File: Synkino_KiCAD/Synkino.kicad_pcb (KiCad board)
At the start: 2 copper layers, 93.3 x 82.3 mm, 183 parts, among them J1 Pwr, J10 EYE8_OUT, J11 EYE4_OUT, J12 2.5mm, J13 EYE5_OUT, J2 2.5mm, J3 3.5mm, J4 Micro_SD_Card_Det_Hirose_DM3AT, J5 EYE1_OUT, J6 EYE6_OUT, J7 EYE2_OUT, J8 EYE7_OUT, J9 EYE3_OUT, Q1 IRF7319, Q2 BC847, Q3 IRLML2244, SW1 SW_Push, SW2 Rotary_Encoder_Switch, SW3 SW_Push, U1 MCP1702T-5002E/MB, U10 ATMEGA328P-AU, U11 QRE1113, U12 QRE1113, U13 QRE1113, U14 QRE1113, U15 QRE1113, U16 QRE1113, U17 24LC256, U18 QRE1113, U2 ATMEGA328P-AU, U3 74HC4050, U4 SPIOLED128x64, U5 AP7312-1833W6-7, U6 74HC14, U7 VS1053B, U8 MAX4741, U9 QRE1113, X1 FTDIconn, X2 ICSP, X3 FTDIconn, X4 ICSP, Y1 16Mhz, Y2 12.288MHz, Y3 16Mhz

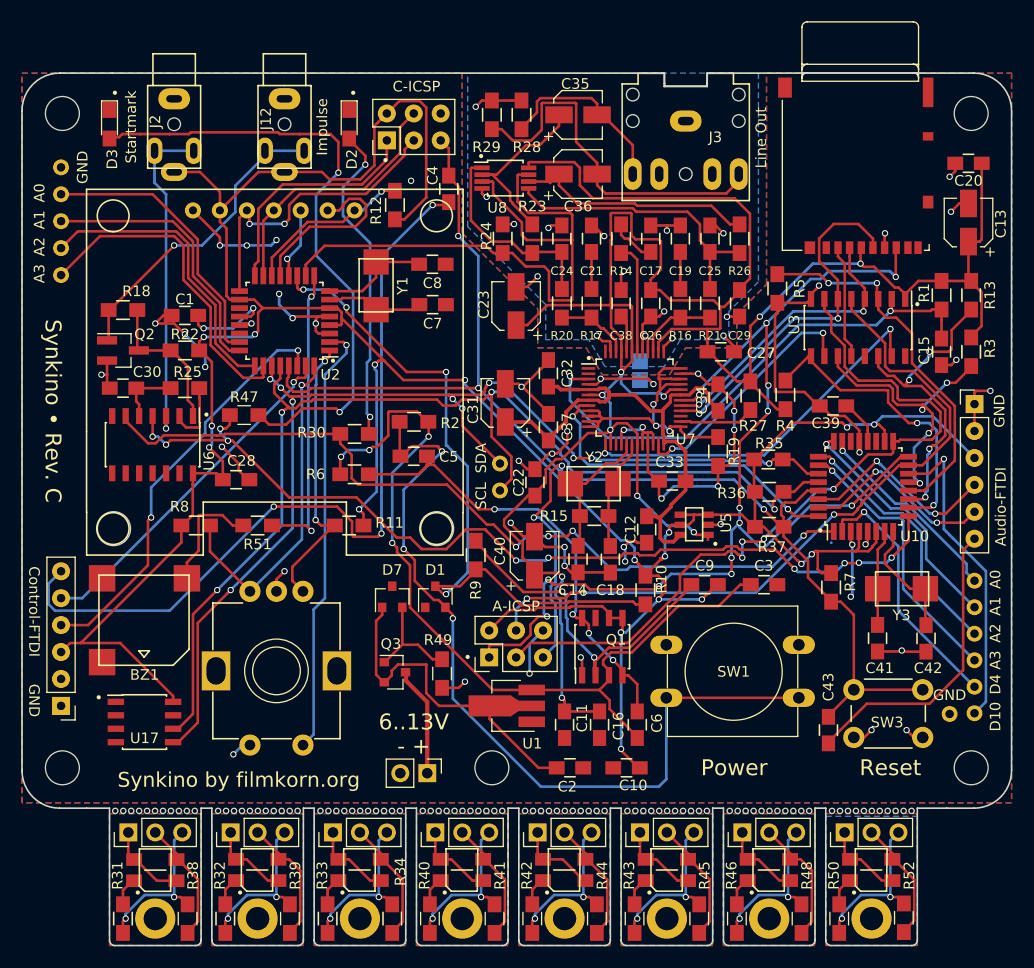
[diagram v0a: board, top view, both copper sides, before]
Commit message: Fixing traces too close to screws
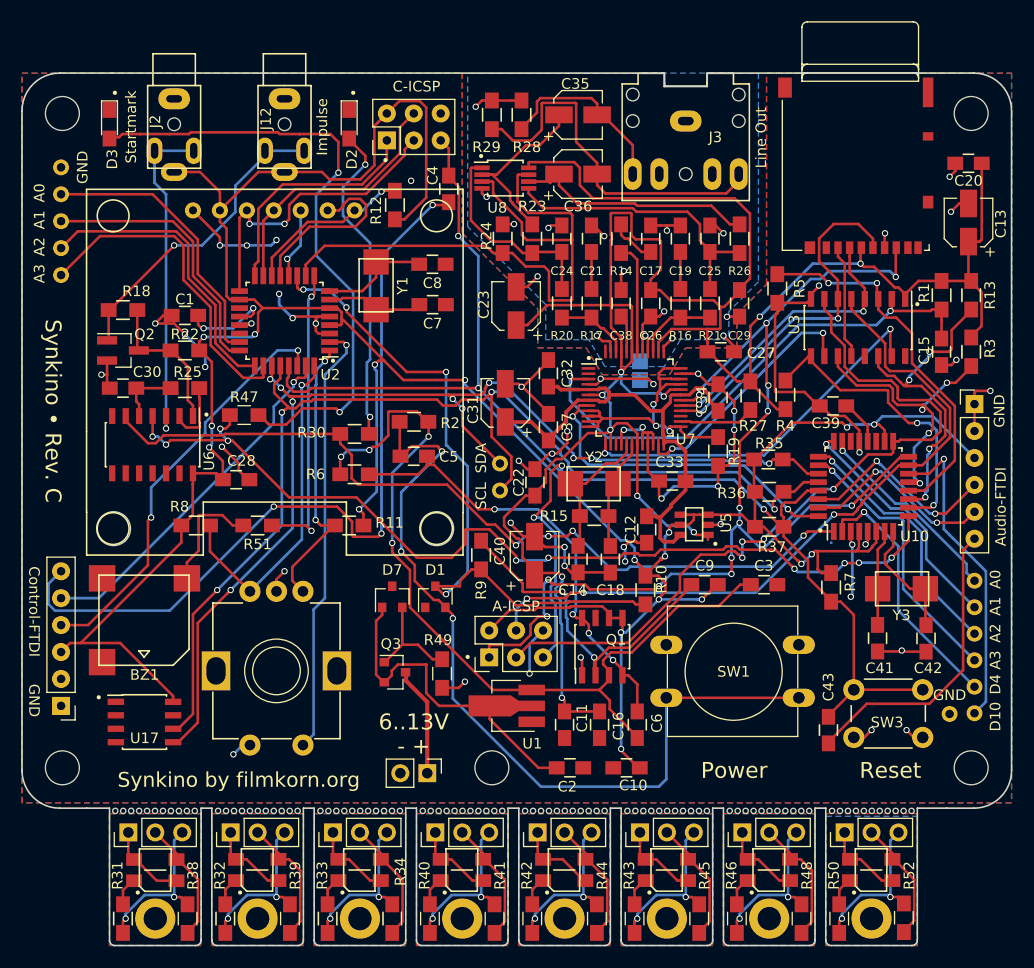
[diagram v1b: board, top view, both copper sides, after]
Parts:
- moved R9 0.51 mm to (110.0, 83.6)
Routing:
- net /Startmark: track 88.6 -> 90.3 mm
- net /CTRL_TXD: track 33.0 -> 33.9 mm

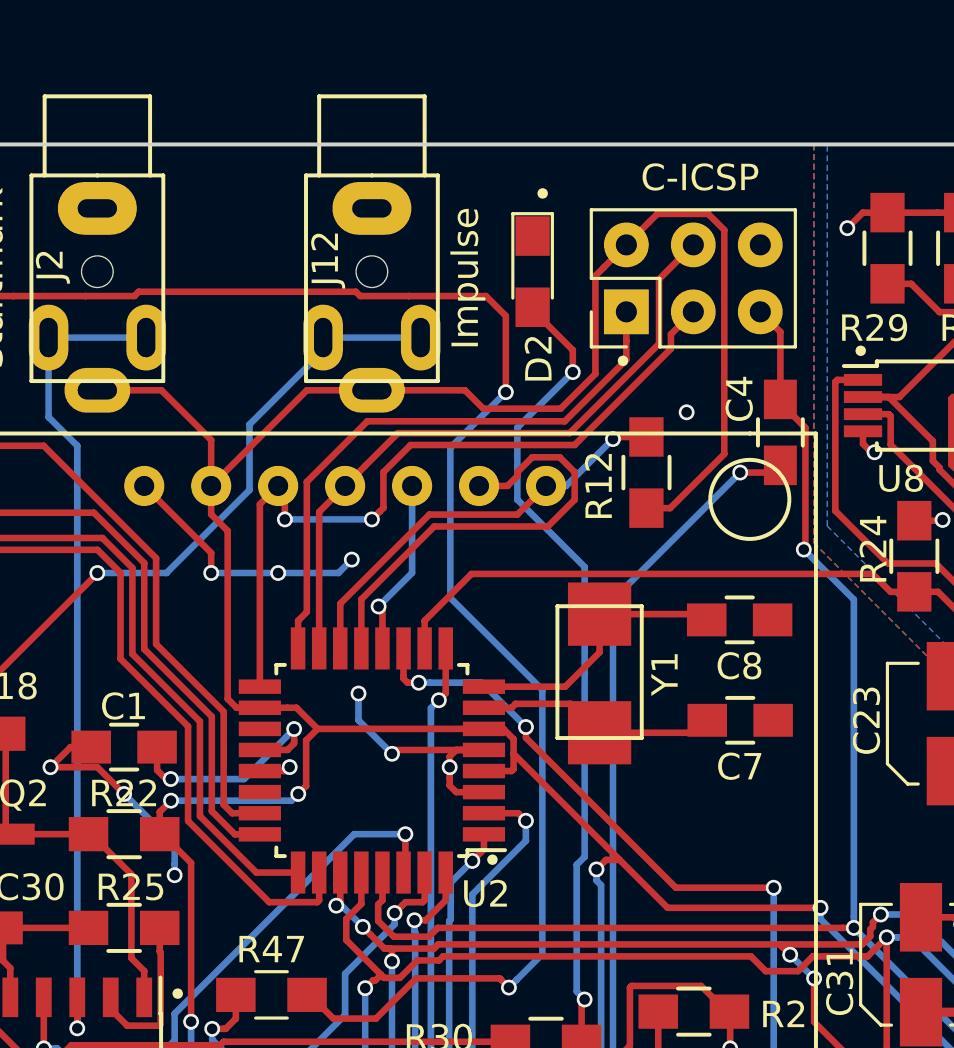
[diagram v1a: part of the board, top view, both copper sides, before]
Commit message: Add 5V out, Add Pulldown-R for ICSP / OLED compat
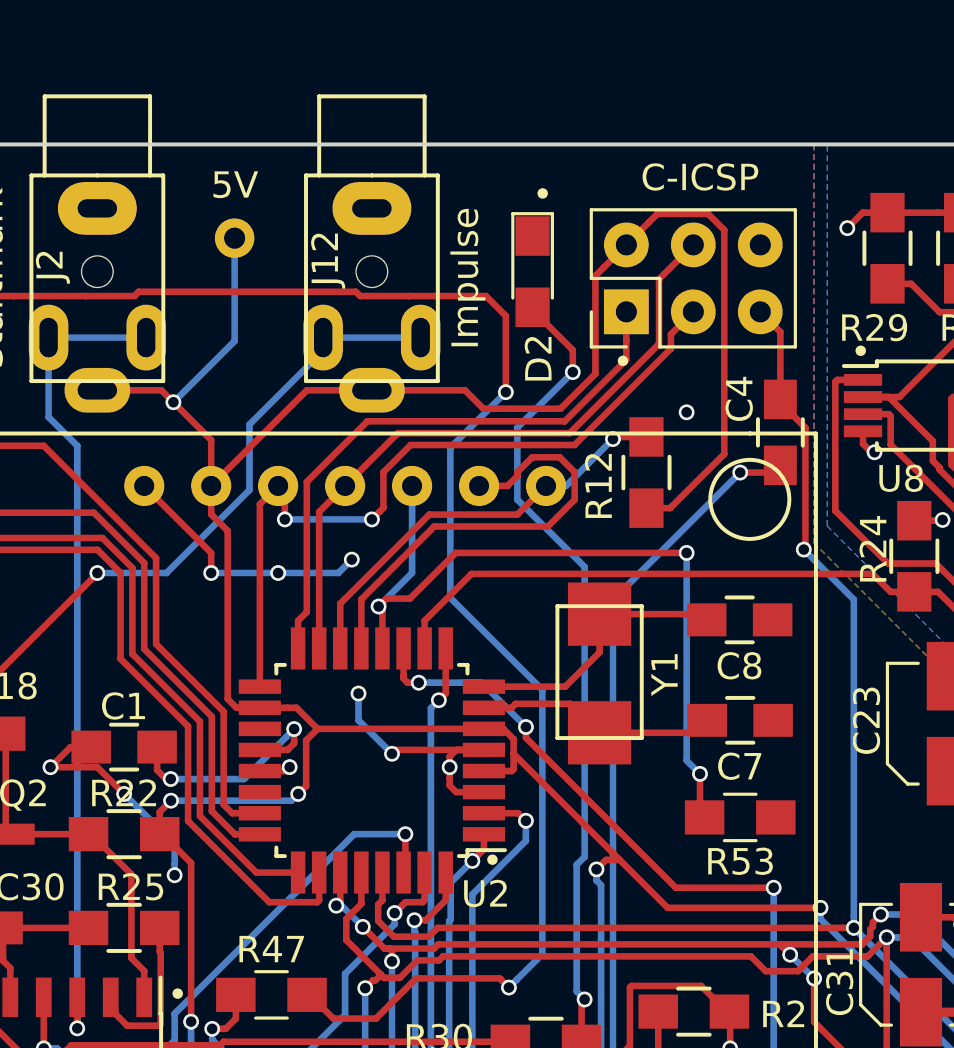
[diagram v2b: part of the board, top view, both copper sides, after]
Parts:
- added 5V: 5V, Measurement_Points:Measurement_Point_Round-TH_Small, F.Cu at (86.2, 41.7)
- added R53: 10k, Resistors_SMD:R_0805_HandSoldering, F.Cu at (105.4, 63.6)
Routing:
- net /OLED_RES: track 6.75 -> 29.6 mm, vias 1 -> 3
- net +5V: track 298.9 -> 306.1 mm, vias 18 -> 19
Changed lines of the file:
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@@
 (kicad_pcb (version 4) (host pcbnew 4.0.7)
   (general
-    (links 384)
-    (no_connects 0)
-    (area 57.856429 32.843999 168.838572 132.270286)
+    (links 387)
+    (no_connects 1)
+    (area 66.599999 38.024999 160.095001 120.471001)
     (thickness 1.6)
     (drawings 107)
-    (tracks 2329)
+    (tracks 2343)
     (zones 0)
-    (modules 183)
+    (modules 185)
     (nets 135)
   )
@@
     )
   )
+  (module Measurement_Points:Measurement_Point_Round-TH_Small (layer F.Cu)
+    (at 86.233 41.656)
+    (descr "Mesurement Point, Square, Trough Hole,  DM 1.5mm, Drill 0.8mm,")
+    (tags "Mesurement Point Round Trough Hole 1.5mm Drill 0.8mm")
+    (attr virtual)
+    (fp_text reference 5V (at 0 -2) (layer F.SilkS)
+      (effects (font (size 1 1) (thickness 0.15)))
+    )
+    (fp_text value 5V (at 0 2) (layer F.Fab)
+      (effects (font (size 1 1) (thickness 0.15)))
+    )
+    (fp_circle (center 0 0) (end 1 0) (layer F.CrtYd) (width 0.05))
+    (pad 1 thru_hole circle (at 0 0) (size 1.5 1.5) (drill 0.8) (layers *.Cu *.Mask)
+      (net 10 +5V))
+  )
+  (module Resistors_SMD:R_0805_HandSoldering (layer F.Cu)
+    (at 105.41 63.627 180)
+    (descr "Resistor SMD 0805, hand soldering")
+    (tags "resistor 0805")
+    (attr smd)
+    (fp_text reference R53 (at 0 -1.7 180) (layer F.SilkS)
+      (effects (font (size 1 1) (thickness 0.15)))
+    )
+    (fp_text value 10k (at 0 1.75 180) (layer F.Fab)
+      (effects (font (size 1 1) (thickness 0.15)))
+    )
+    (fp_text user %R (at 0 0 180) (layer F.Fab)
+      (effects (font (size 0.5 0.5) (thickness 0.075)))
+    )
+    (fp_line (start -1 0.62) (end -1 -0.62) (layer F.Fab) (width 0.1))
+    (fp_line (start 1 0.62) (end -1 0.62) (layer F.Fab) (width 0.1))
+    (fp_line (start 1 -0.62) (end 1 0.62) (layer F.Fab) (width 0.1))
+    (fp_line (start -1 -0.62) (end 1 -0.62) (layer F.Fab) (width 0.1))
+    (fp_line (start 0.6 0.88) (end -0.6 0.88) (layer F.SilkS) (width 0.12))
+    (fp_line (start -0.6 -0.88) (end 0.6 -0.88) (layer F.SilkS) (width 0.12))
+    (fp_line (start -2.35 -0.9) (end 2.35 -0.9) (layer F.CrtYd) (width 0.05))
+    (fp_line (start -2.35 -0.9) (end -2.35 0.9) (layer F.CrtYd) (width 0.05))
+    (fp_line (start 2.35 0.9) (end 2.35 -0.9) (layer F.CrtYd) (width 0.05))
+    (fp_line (start 2.35 0.9) (end -2.35 0.9) (layer F.CrtYd) (width 0.05))
+    (pad 1 smd rect (at -1.35 0 180) (size 1.5 1.3) (layers F.Cu F.Paste F.Mask)
+      (net 2 GND))
+    (pad 2 smd rect (at 1.35 0 180) (size 1.5 1.3) (layers F.Cu F.Paste F.Mask)
+      (net 62 /OLED_RES))
+    (model ${KISYS3DMOD}/Resistors_SMD.3dshapes/R_0805.wrl
+      (at (xyz 0 0 0))
+      (scale (xyz 1 1 1))
+      (rotate (xyz 0 0 0))
+    )
+  )
   (gr_text • (at 73.914 97.028) (layer F.SilkS)
     (effects (font (size 1 1) (thickness 0.2)))
@@
   (segment (start 98.774 58.668) (end 100.076 57.366) (width 0.25) (layer F.Cu) (net 9))
   (segment (start 100.076 57.366) (end 100.076 55.916) (width 0.25) (layer F.Cu) (net 9))
+  (segment (start 85.344 49.312) (end 83.911 47.879) (width 0.25) (layer F.Cu) (net 10))
+  (segment (start 83.911 47.879) (end 83.458 47.426) (width 0.25) (layer F.Cu) (net 10))
+  (via (at 83.911 47.879) (size 0.6) (drill 0.4) (layers F.Cu B.Cu) (net 10))
+  (segment (start 86.233 41.656) (end 86.233 45.557) (width 0.25) (layer B.Cu) (net 10))
+  (segment (start 86.233 45.557) (end 83.911 47.879) (width 0.25) (layer B.Cu) (net 10))
   (segment (start 84.582 71.374) (end 84.582 65.352) (width 0.25) (layer F.Cu) (net 10))
   (segment (start 84.582 65.352) (end 83.492 64.262) (width 0.25) (layer F.Cu) (net 10))
@@
   (segment (start 70.358 92.71) (end 71.207999 91.860001) (width 0.25) (layer F.Cu) (net 10))
   (segment (start 71.207999 91.860001) (end 72.223999 91.860001) (width 0.25) (layer F.Cu) (net 10))
-  (segment (start 85.344 49.312) (end 83.458 47.426) (width 0.25) (layer F.Cu) (net 10))
   (segment (start 98.886 79.664204) (end 98.770531 79.548735) (width 0.25) (layer F.Cu) (net 10))
   (segment (start 100.133989 66.197314) (end 100.133989 77.585279) (width 0.25) (layer B.Cu) (net 10))
@@
   (segment (start 140.418 76.689) (end 140.75 76.689) (width 0.25) (layer F.Cu) (net 61))
   (segment (start 140.75 76.689) (end 141.8 76.689) (width 0.25) (layer F.Cu) (net 61))
+  (segment (start 103.886 61.976) (end 103.886 63.453) (width 0.25) (layer F.Cu) (net 62))
+  (segment (start 103.886 63.453) (end 104.06 63.627) (width 0.25) (layer F.Cu) (net 62))
+  (segment (start 103.378 53.594) (end 103.378 61.468) (width 0.25) (layer B.Cu) (net 62))
+  (segment (start 103.378 61.468) (end 103.886 61.976) (width 0.25) (layer B.Cu) (net 62))
+  (via (at 103.886 61.976) (size 0.6) (drill 0.4) (layers F.Cu B.Cu) (net 62))
+  (segment (start 92.882999 55.326001) (end 94.615 53.594) (width 0.25) (layer F.Cu) (net 62))
+  (segment (start 94.615 53.594) (end 103.378 53.594) (width 0.25) (layer F.Cu) (net 62))
+  (via (at 103.378 53.594) (size 0.6) (drill 0.4) (layers F.Cu B.Cu) (net 62))
+  (segment (start 91.694 55.626) (end 91.993999 55.326001) (width 0.25) (layer F.Cu) (net 62))
+  (segment (start 91.993999 55.326001) (end 92.882999 55.326001) (width 0.25) (layer F.Cu) (net 62))
   (segment (start 91.694 55.626) (end 92.964 54.356) (width 0.25) (layer B.Cu) (net 62))
   (segment (start 92.964 54.356) (end 92.964 51.054) (width 0.25) (layer B.Cu) (net 62))

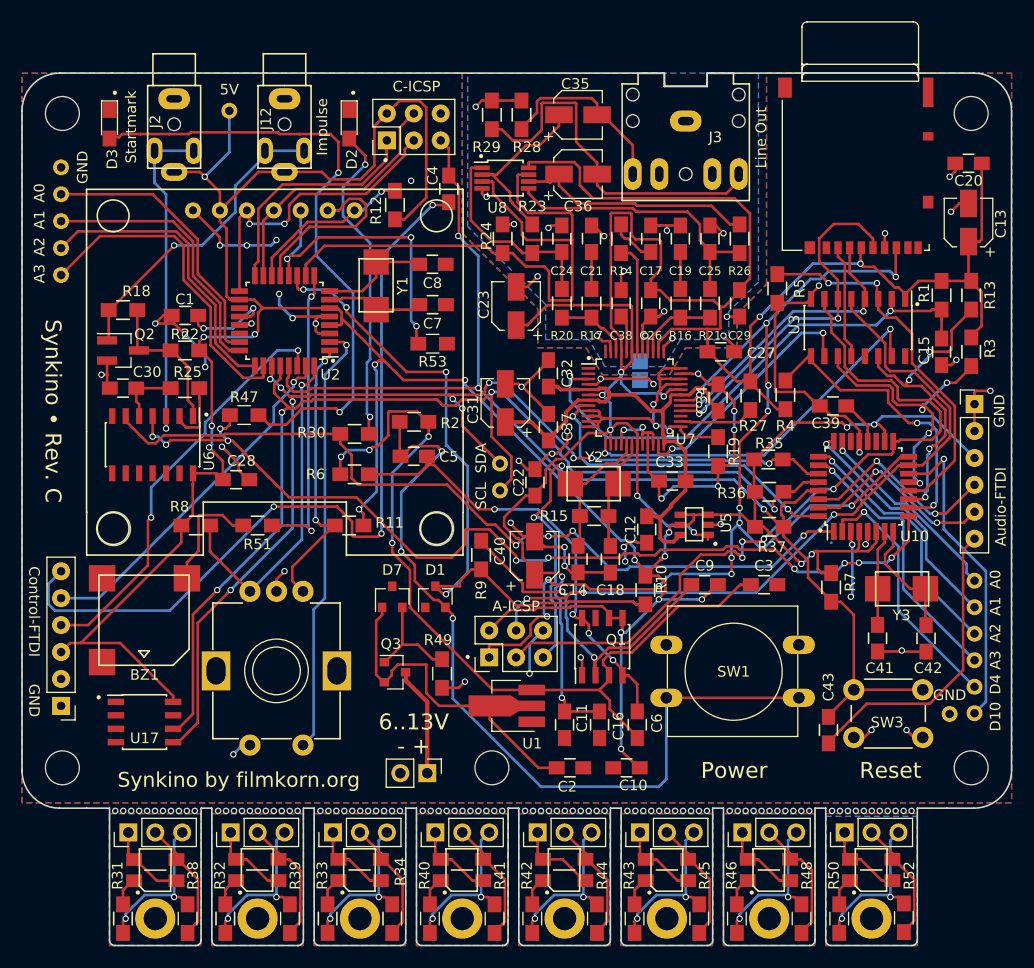
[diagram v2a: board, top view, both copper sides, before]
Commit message: Mark GND on FTDI
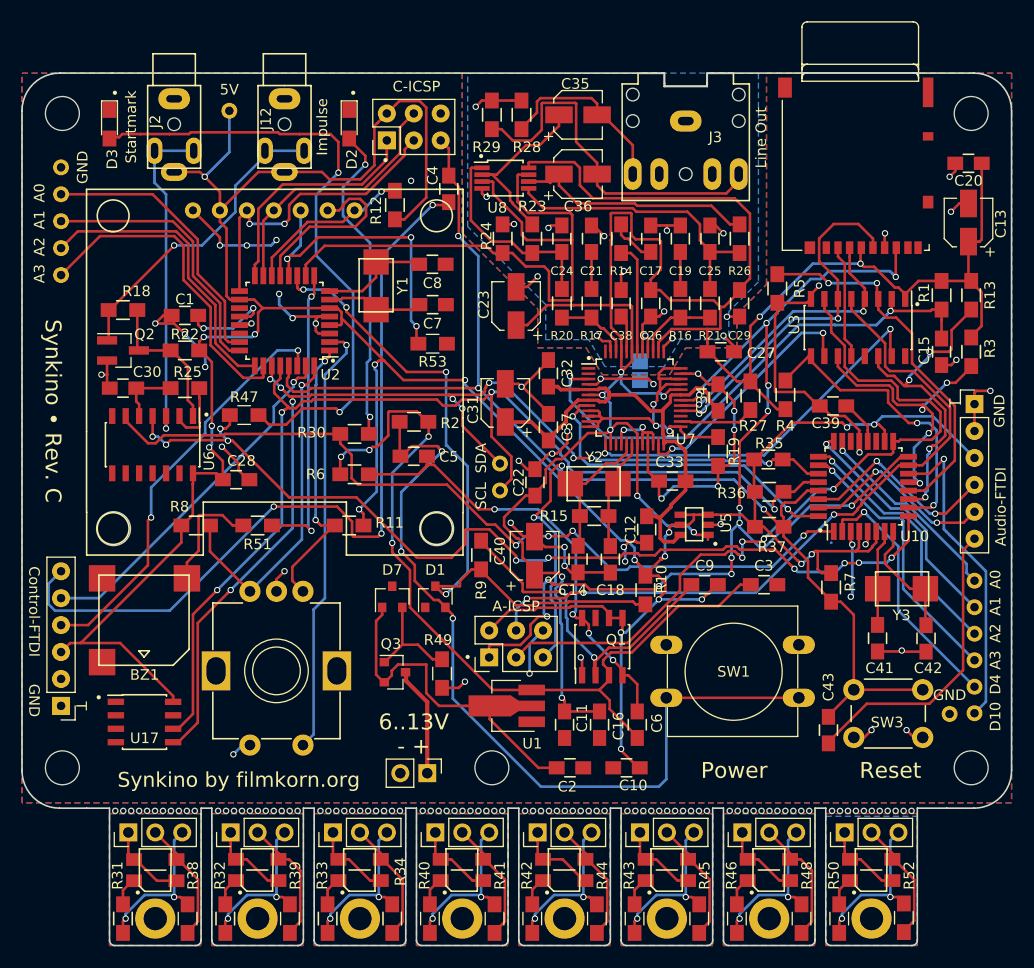
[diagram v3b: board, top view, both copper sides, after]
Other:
- board text added: "T"
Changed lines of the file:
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@@
     (area 66.599999 38.024999 160.095001 120.471001)
     (thickness 1.6)
-    (drawings 107)
+    (drawings 109)
     (tracks 2343)
     (zones 0)
@@
     )
   )
+  (gr_text T (at 154.686 69.215 90) (layer F.SilkS)
+    (effects (font (size 1 1) (thickness 0.2)))
+  )
+  (gr_text T (at 72.263 97.79 270) (layer F.SilkS)
+    (effects (font (size 1 1) (thickness 0.2)))
+  )
   (gr_text • (at 73.914 97.028) (layer F.SilkS)

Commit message: 5 and 3v3 out
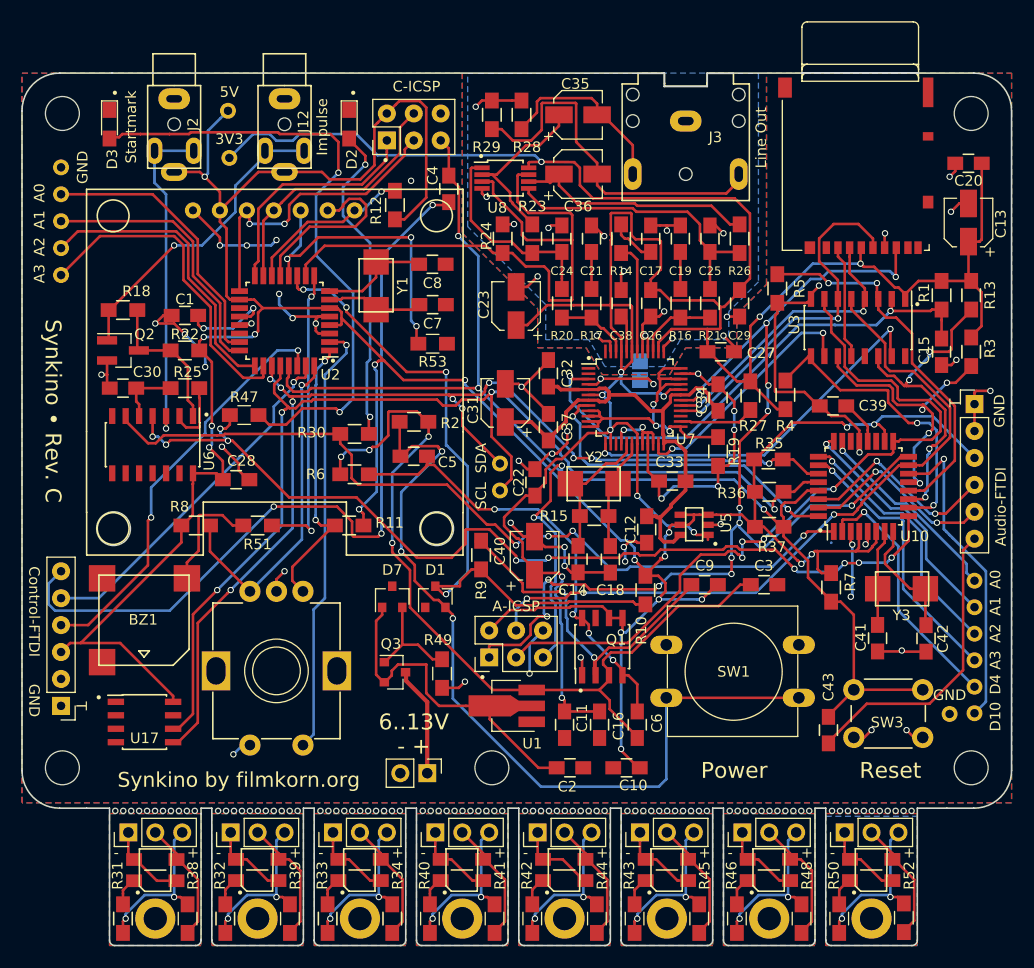
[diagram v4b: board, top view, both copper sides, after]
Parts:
- added 3V3: 3V3, Measurement_Points:Measurement_Point_Round-TH_Small, F.Cu at (86.2, 46.1)
- J3: footprint lib_fp:SJ1-352XNG -> lib_fp:SJ1-352XNG-3pin
- moved 5V 0.13 mm to (86.1, 41.7)
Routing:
- net +3V3: track 235.6 -> 267.5 mm, vias 10 -> 11
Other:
- board text added: "+"
- board text added: "-"
- board text added: "In"
- board text added: "^"

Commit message: Final tweaks for Rev C
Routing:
- net +3V3: track 267.5 -> 284.0 mm
- net Net-(CA0-Pad1): track 26.6 -> 27.1 mm
- net Net-(CA1-Pad1): track 25.9 -> 26.4 mm
- net Net-(CA2-Pad1): track 28.2 -> 28.7 mm
- net Net-(CA3-Pad1): track 31.2 -> 31.8 mm
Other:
- board text added: "3V3"
- board text added: "5V"

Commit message: RevD, baby
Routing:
- net Net-(C5-Pad2): track 79.1 -> 70.2 mm
- net Net-(C2-Pad1): track 36.8 -> 34.6 mm
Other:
- board text added: "Synkino • Rev. D"
- board text removed: "Synkino • Rev. C"

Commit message: KiCad 5 version, .gitignore
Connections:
- net /~PWR_OFF renamed /~{PWR_OFF}
- net /~RST renamed /~{RST}
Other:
- net class Default removed
